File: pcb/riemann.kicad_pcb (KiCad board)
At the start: 2 copper layers, 266.7 x 95.2 mm, 285 parts, among them J1 Cortex Debug, J2 USB-C, SW1 Reset, SW10 Keyswitch, SW11 Keyswitch, SW12 Keyswitch, SW13 Keyswitch, SW14 Keyswitch, SW15 Keyswitch, SW16 Keyswitch, SW17 Keyswitch, SW18 Keyswitch, SW19 Keyswitch, SW2 DFU, SW20 Keyswitch, SW21 Keyswitch, SW22 Keyswitch, SW23 Keyswitch, SW24 Keyswitch, SW25 Keyswitch, SW26 Keyswitch, SW27 Keyswitch, SW28 Keyswitch, SW29 Keyswitch, SW3 Keyswitch, SW30 Keyswitch, SW31 Keyswitch, SW32 Keyswitch, SW33 Keyswitch, SW34 Keyswitch, SW35 Keyswitch, SW36 Keyswitch, SW37 Keyswitch, SW38 Keyswitch, SW39 Keyswitch, SW4 Keyswitch, SW40 Keyswitch, SW41 Keyswitch, SW42 Keyswitch, SW43 Keyswitch, SW44 Keyswitch, SW45 Keyswitch, SW46 Keyswitch, SW47 Keyswitch, SW48 Keyswitch, SW49 Keyswitch, SW5 Keyswitch, SW50 Keyswitch, SW51 Keyswitch, SW52 Keyswitch, SW53 Keyswitch, SW54 Keyswitch, SW55 Keyswitch, SW56 Keyswitch, SW57 Keyswitch, SW58 Keyswitch, SW59 Keyswitch, SW6 Keyswitch, SW60 Keyswitch, SW61 Keyswitch, SW62 Keyswitch, SW7 Keyswitch, SW8 Keyswitch, SW9 Keyswitch, U1 AZ1117-3.3, U2 MIC94093YC6, U3 ATSAMD21G15A-A, U4 74LVC2T45DC, X1 ASTMHT-48.000MHz

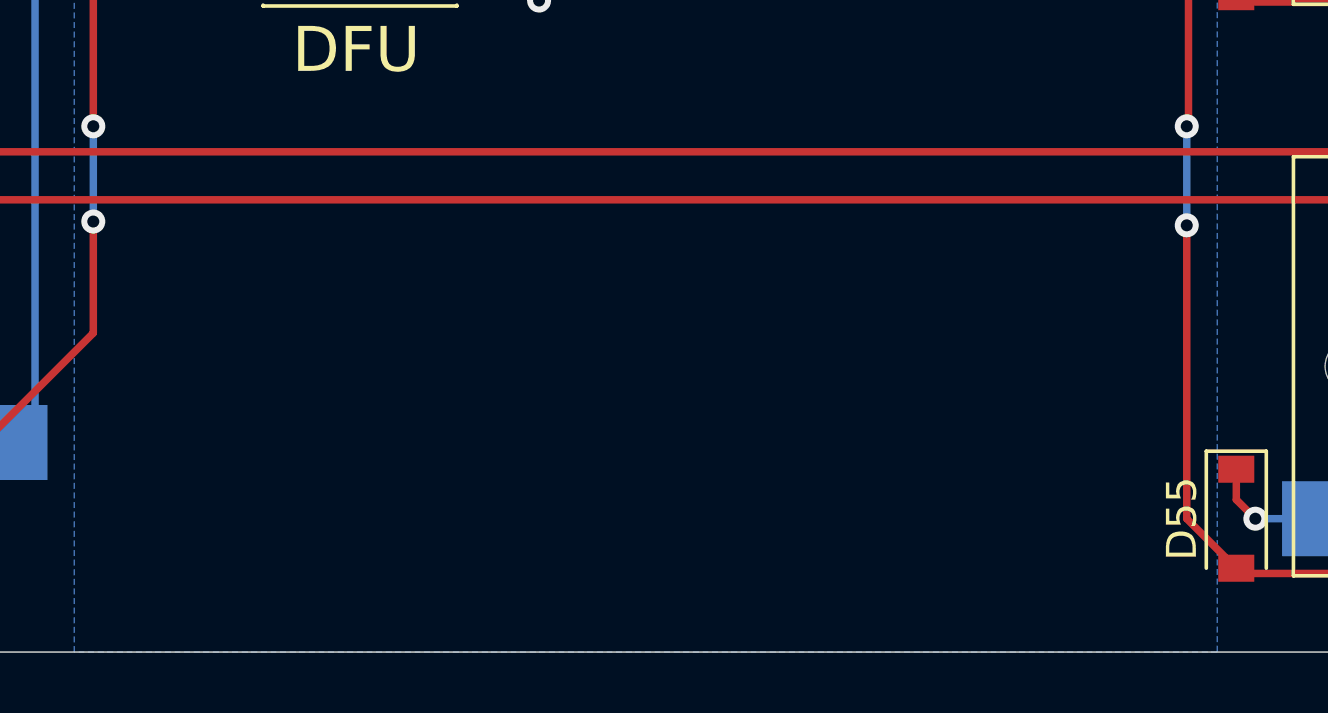
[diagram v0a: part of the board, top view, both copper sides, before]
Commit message: Add branding to PCB
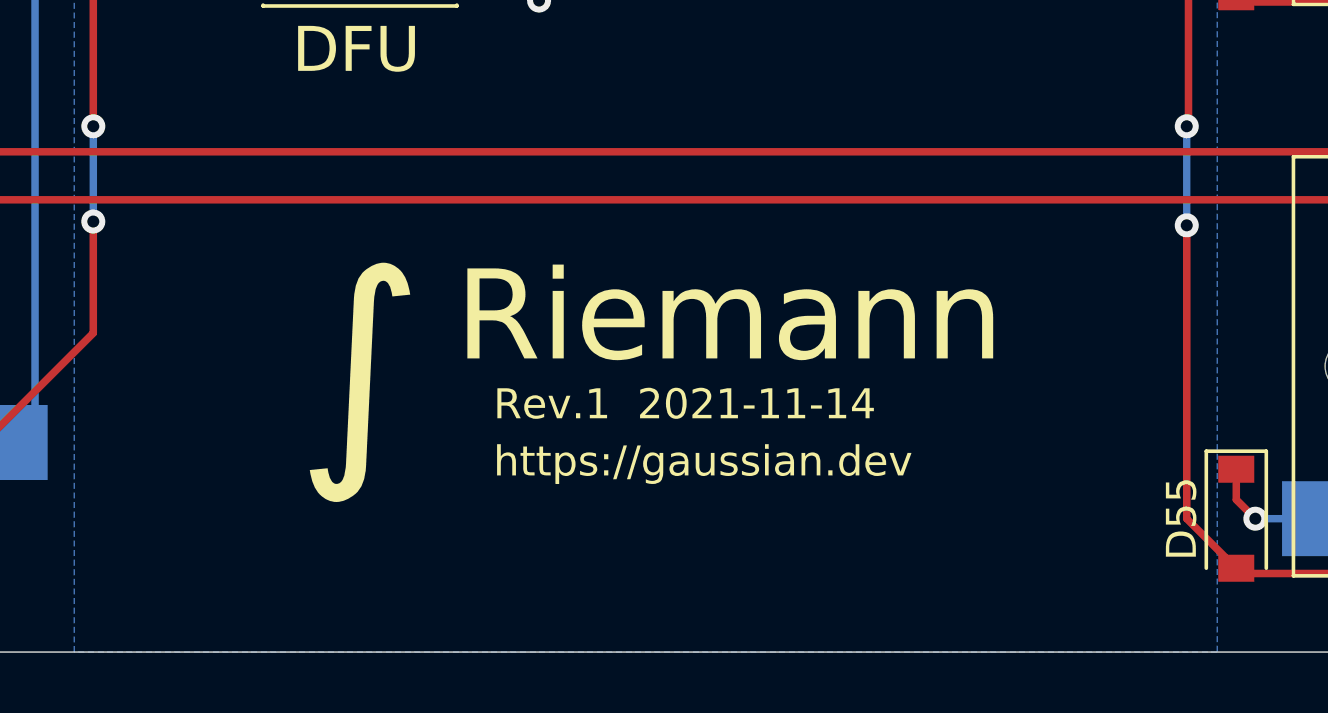
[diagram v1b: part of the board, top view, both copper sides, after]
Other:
- board text added: "Rev.1 2021-11-14"
- board text added: "Riemann"
- board text added: "https://gaussian.dev"
- board text added: "∫"
